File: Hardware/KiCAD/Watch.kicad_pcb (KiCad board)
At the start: 2 copper layers, 32 x 32 mm, 74 parts, among them IC101 TCR2LF33,LM_CT, IC102 PCF85063AT_AY, IC103 SFH_5711-2_3-Z, IC201 IS31FL3235A-QFLS2-TR, J101 Conn_01x02, J102 Conn_01x01, J103 Conn_01x01, J104 Conn_ARM_JTAG_SWD_10, J105 Conn_01x02, U101 ATSAM4LS2AA-AU, U102 MCP73831-2-OT, Y101 CM8V-T1A-32.768kHz-4pF-20PPM-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

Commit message: Layout almost complete, hitting some snags with routing LED driver
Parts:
- removed C108: 0.1uF, SamacSys_Parts:CAPC1005X55N
- removed R201, R202: 4.7k, Resistor_SMD:R_01005_0402Metric
- removed TP101, TP102, TP104, TP105: TestPoint, TestPoint:TestPoint_Pad_D1.0mm
- C105, C106, C201, C202, D101, IC102, J101, J102, J103, J104, J105, TP103, Y101: moved to B.Cu
- R101, R102, R106, R113, R114: footprint Resistor_SMD:R_01005_0402Metric -> Resistor_SMD:R_0402_1005Metric
- R103: value 4.7k -> 10k; footprint Resistor_SMD:R_01005_0402Metric -> Resistor_SMD:R_0402_1005Metric
- R104, R105: value 4.7k -> 10k; footprint Resistor_SMD:R_01005_0402Metric -> Resistor_SMD:R_0402_1005Metric; moved to B.Cu
- R107, R108, R109, R110, R111, R112, R203: footprint Resistor_SMD:R_01005_0402Metric -> Resistor_SMD:R_0402_1005Metric; moved to B.Cu
- R204: value 100k -> 10k; footprint Resistor_SMD:R_01005_0402Metric -> Resistor_SMD:R_0402_1005Metric
- moved R113 65.5 mm to (138.8, 96.1), turned to 180 degrees
- moved R114 65.5 mm to (138.8, 97.3)
- moved R109 58.7 mm to (144.2, 88.4)
- moved R112 58.5 mm to (144.1, 91.3)
- moved TP103 58.0 mm to (153.4, 88.1)
- moved R111 55.9 mm to (144.1, 89.8)
- moved LED102 55.0 mm to (136.3, 91.3), turned to 90 degrees
- moved R110 54.0 mm to (144.2, 87.1)
- moved R104 52.1 mm to (139.1, 84.8), turned to 180 degrees
- moved C105 51.7 mm to (146.1, 84.8)
- moved IC102 50.3 mm to (139.0, 90.3)
- moved J102 50.0 mm to (157.7, 89.8), turned to 90 degrees
- moved J105 49.7 mm to (155.7, 86.0)
- moved J103 49.7 mm to (157.7, 86.6), turned to 90 degrees
- moved R106 47.7 mm to (138.8, 95.0)
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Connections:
- C201 pad 1: Net-(C201-Pad1) -> +3V3
- C201 pad 2: Net-(C201-Pad2) -> GND
- LED201 pad 1: /leds/OUT1 -> /leds/OUT24
- LED202 pad 1: /leds/OUT2 -> /leds/OUT23
- LED203 pad 1: /leds/OUT3 -> /leds/OUT22
- LED204 pad 1: /leds/OUT4 -> /leds/OUT21
- LED205 pad 1: /leds/OUT5 -> /leds/OUT20
- LED206 pad 1: /leds/OUT6 -> /leds/OUT19
- LED207 pad 1: /leds/OUT7 -> /leds/OUT18
- LED208 pad 1: /leds/OUT8 -> /leds/OUT17
- LED209 pad 1: /leds/OUT9 -> /leds/OUT16
- LED210 pad 1: /leds/OUT10 -> /leds/OUT15
- LED211 pad 1: /leds/OUT12 -> /leds/OUT14
- LED213 pad 1: /leds/OUT14 -> /leds/OUT12
- LED214 pad 1: /leds/OUT15 -> /leds/OUT11
- LED215 pad 1: /leds/OUT16 -> /leds/OUT10
- LED216 pad 1: /leds/OUT17 -> /leds/OUT9
- LED217 pad 1: /leds/OUT18 -> /leds/OUT8
- LED218 pad 1: /leds/OUT19 -> /leds/OUT7
- LED219 pad 1: /leds/OUT20 -> /leds/OUT6
- LED220 pad 1: /leds/OUT21 -> /leds/OUT5
- LED221 pad 1: /leds/OUT21 -> /leds/OUT4
- LED222 pad 1: /leds/OUT22 -> /leds/OUT3
- LED223 pad 1: /leds/OUT23 -> /leds/OUT2
- LED224 pad 1: /leds/OUT24 -> /leds/OUT1
- LED225 pad 1: /leds/OUT25 -> /leds/OUT27
- LED225 pad 5: /leds/OUT27 -> /leds/OUT25
- U101 pad 1: /SW1 -> Net-(U101-Pad1)
- U101 pad 2: /SW2 -> Net-(U101-Pad2)
- U101 pad 35: Net-(U101-Pad35) -> /SW2
- U101 pad 36: Net-(U101-Pad36) -> /SW1
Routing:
- net +3V3: track 0.00 -> 193.4 mm, vias 0 -> 2
- net /leds/OUT23: track 0.00 -> 48.8 mm, vias 0 -> 2
- net /leds/OUT22: track 0.00 -> 46.4 mm, vias 0 -> 2
- net /leds/OUT21: track 0.00 -> 44.7 mm, vias 0 -> 2
- net /leds/OUT18: track 0.00 -> 42.1 mm, vias 0 -> 2
- net /leds/OUT20: track 0.00 -> 41.9 mm, vias 0 -> 2
- net /leds/OUT17: track 0.00 -> 40.5 mm, vias 0 -> 2
- net /leds/OUT19: track 0.00 -> 39.2 mm, vias 0 -> 2
- net /leds/OUT16: track 0.00 -> 38.6 mm, vias 0 -> 2
- net +BATT: track 0.00 -> 37.7 mm, vias 0 -> 1
- net /leds/OUT15: track 0.00 -> 37.4 mm, vias 0 -> 2
- net /leds/OUT14: track 0.00 -> 36.0 mm, vias 0 -> 2
- net /leds/OUT24: track 0.00 -> 33.9 mm, vias 0 -> 2
- net /leds/OUT13: track 0.00 -> 26.0 mm
- net /leds/OUT12: track 0.00 -> 23.0 mm
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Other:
- net class Default: clearance 0.2 -> 0.15
- rule trace_clearance: 0.2 -> 0.15
- rule trace_min: 0.2 -> 0.15
- rule via_min_size: 0.4 -> 0.3
- board text added: "v1.0 Cade Walton"

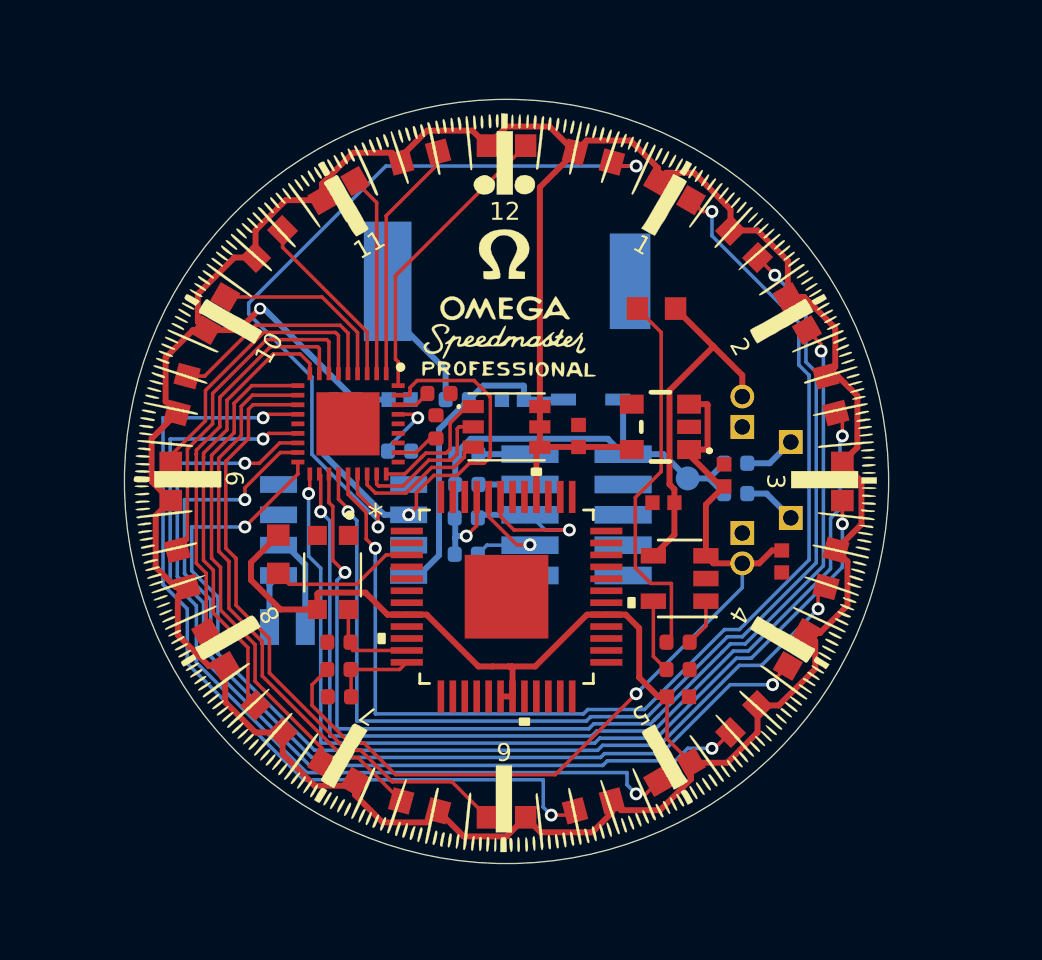
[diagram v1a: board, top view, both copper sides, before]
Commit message: Signals routed. Ground pours in progress
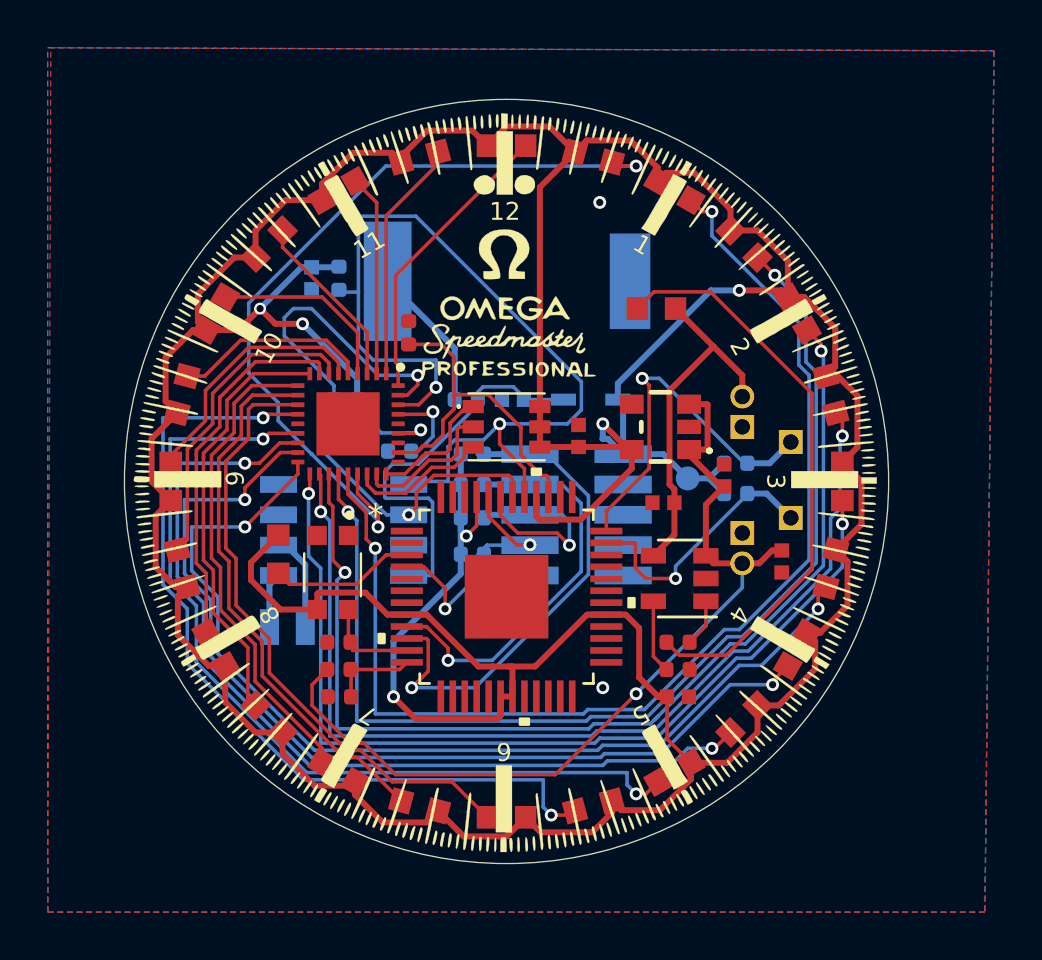
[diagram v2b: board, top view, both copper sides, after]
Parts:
- R103: moved to B.Cu
- moved R103 6.39 mm to (138.8, 79.8), turned to 270 degrees
- moved C202 6.27 mm to (137.7, 79.8), turned to 270 degrees
- moved R204 4.10 mm to (141.7, 82.0)
- moved R105 0.38 mm to (144.1, 84.8)
- moved R111 0.25 mm to (144.4, 89.8)
- moved R112 0.25 mm to (144.4, 91.3)
- moved R109 0.23 mm to (144.4, 88.4)
- moved R110 0.23 mm to (144.4, 87.1)
- turned R203 to 0 degrees
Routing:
- net /SDA: track 1.60 -> 39.0 mm, vias 0 -> 2
- net +3V3: track 193.4 -> 223.5 mm, vias 2 -> 7
- net /JTAG_TMS: track 2.16 -> 21.2 mm, vias 0 -> 1
- net /JTAG_TCK: track 2.16 -> 17.2 mm, vias 0 -> 1
- net /SW1: track 2.19 -> 15.3 mm, vias 0 -> 1
- net /SDB: track 1.83 -> 14.7 mm
- net /SW2: track 2.24 -> 11.2 mm, vias 0 -> 1
- net Net-(LED101-Pad1): track 16.0 -> 24.8 mm
- net /JTAG_RESET: track 0.00 -> 6.98 mm, vias 0 -> 1
- net /SCL: track 19.1 -> 26.0 mm, vias 1 -> 2
- net Net-(C105-Pad2): track 13.4 -> 16.7 mm
- net Net-(C106-Pad1): track 5.96 -> 7.40 mm
- net /leds/OUT6: track 9.46 -> 8.23 mm
- net /leds/OUT7: track 11.8 -> 10.7 mm
- net /leds/OUT8: track 14.3 -> 13.3 mm
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- added copper zone on B.Cu, net GND
- added copper zone on F.Cu, net GND

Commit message: Layout complete, pending inspection and purchase
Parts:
- moved R104 1.58 mm to (140.5, 84.2), turned to 0 degrees
- moved C201 1.57 mm to (140.5, 85.6)
- moved R114 1.52 mm to (138.8, 95.8)
- moved R113 0.66 mm to (138.8, 96.8)
- moved R105 0.38 mm to (144.2, 84.5)
- moved C105 0.38 mm to (146.1, 84.5)
- moved R106 0.26 mm to (138.8, 94.7)
- turned C101 to 180 degrees
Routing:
- net GND: track 0.00 -> 25.8 mm, vias 2 -> 15
- net +BATT: track 37.7 -> 41.3 mm
- net /leds/OUT1: track 12.4 -> 13.8 mm
- net /leds/OUT23: track 48.8 -> 50.0 mm
- net /leds/OUT22: track 46.4 -> 47.5 mm
- net /SW1: track 15.3 -> 16.2 mm
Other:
- net class Default: via_dia 0.8 -> 0.54; via_drill 0.4 -> 0.3

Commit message: Release v1.0
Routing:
- net GND: vias 15 -> 16
